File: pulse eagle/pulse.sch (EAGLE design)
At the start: 18 parts, among them J1 ISP Touch, U1 ATMEGA328P, Y1 16MHz

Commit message: Adding extra stem led and three extra petal leds. Needs routing.
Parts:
- added JP7, JP9: (no value), SparkFun-Connectors:M03POLAR_LOCK
- added JP8: M023.5MM_LOCK, SparkFun-Connectors:M023.5MM_LOCK
- added R3: 220, resistor:R-US_R0805
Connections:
- new net N$1: JP9.2, R3.2
- new net PETALWHITE: JP7.1, JP7.2, JP7.3, U1.PB1(OC1A)
- new net STEMLED2: R3.1, U1.PD7(AIN1)
- net 12V: now also JP8.2
- net GND: now also JP8.1, JP9.1
- net STEMLED: now also U1.PB0(ICP); no longer U1.PB1(OC1A)
- net VCC: now also JP9.3
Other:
- moved on the sheet: JP1, JP2, JP3, JP4, R1, SL2

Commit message: Revision 5 of the board, with 4 x Petals, 2 x Stem.
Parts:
- JP1: value (none) -> Power
- JP4, JP9: value (none) -> Stem
- JP6: value M023.5MM_LOCK -> Petal Center
- JP8: value M023.5MM_LOCK -> Petal Color
- SL2: value (none) -> Pulse Sensor
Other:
- note added: "Pulse & Bloom, 2014"
- moved on the sheet: C1, C10, C11, J1, JP1, JP2, JP3, JP4, JP7, JP8, R1, R2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

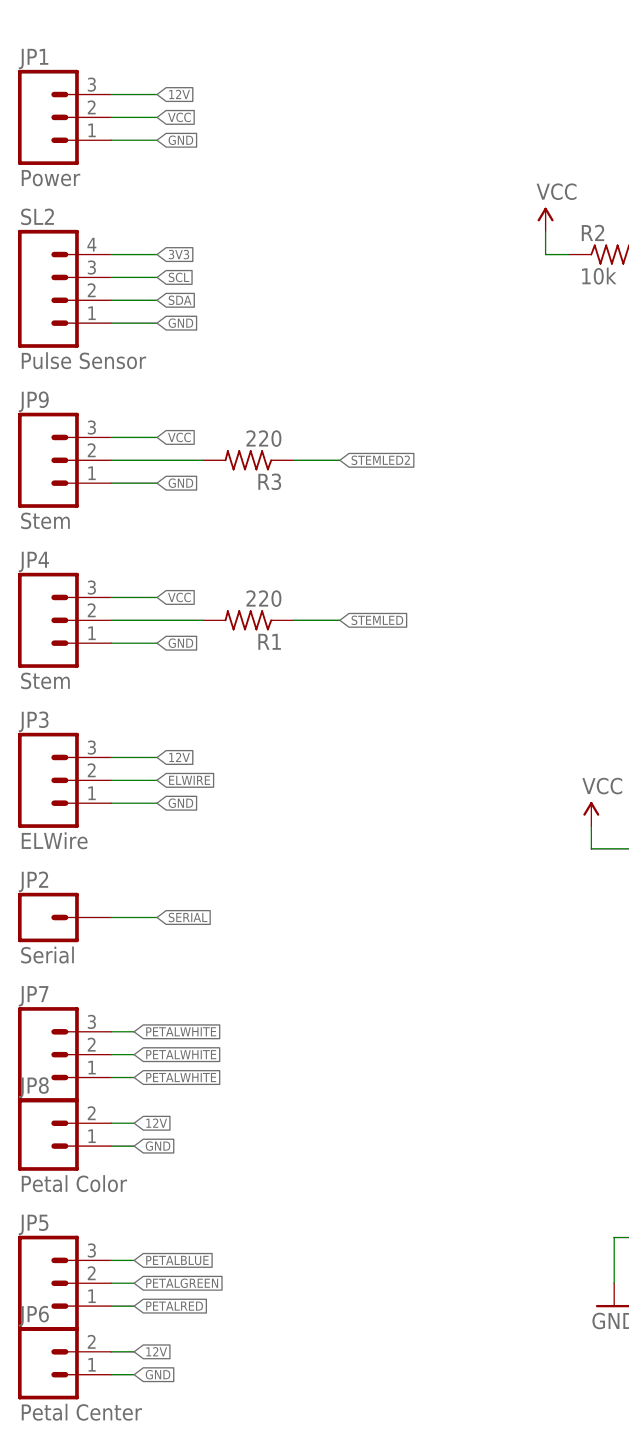
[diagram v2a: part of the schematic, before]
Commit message: Adding extra gnd pins for picobucks. probably going to need more picobucks.
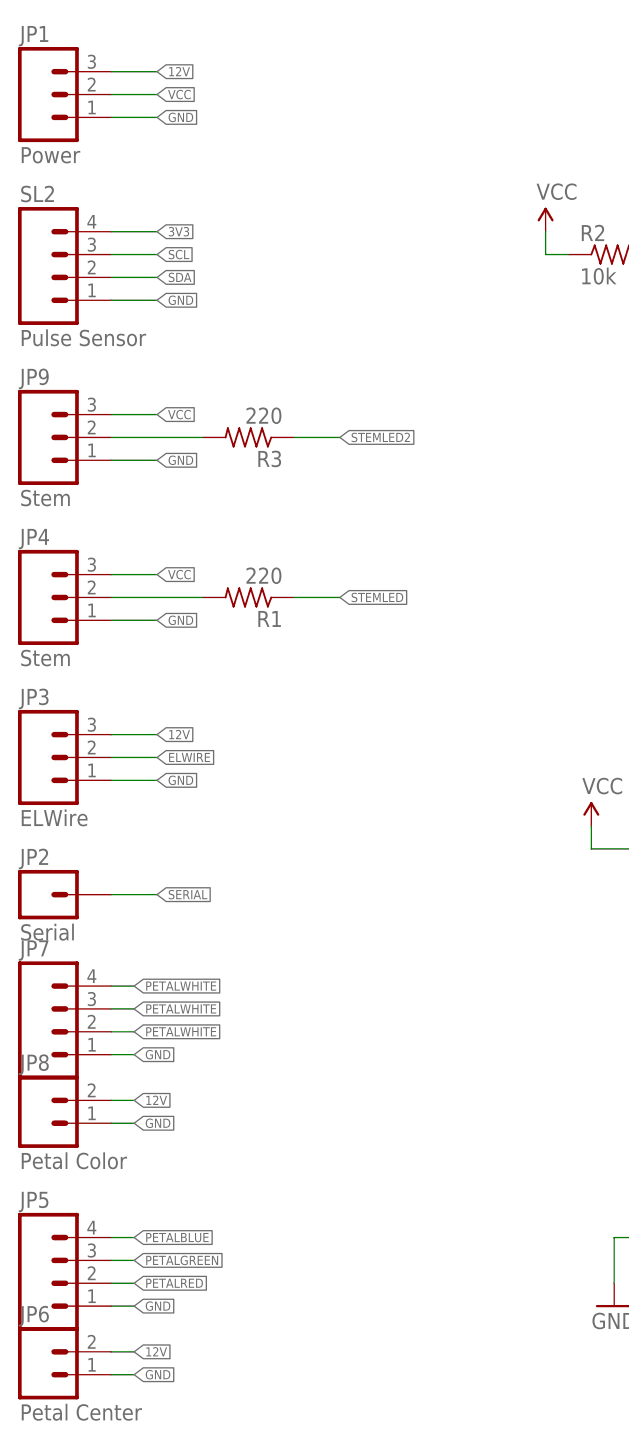
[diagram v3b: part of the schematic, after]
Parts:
- JP5: device SparkFun-Connectors:M03POLAR_LOCK -> SparkFun-Connectors:M04POLAR_LOCK
- JP7: device SparkFun-Connectors:M03POLAR_LOCK -> SparkFun-Connectors:M04POLAR
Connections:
- net GND: now also JP5.1, JP7.1
- net PETALBLUE: now also JP5.4; no longer JP5.3
- net PETALGREEN: now also JP5.3; no longer JP5.2
- net PETALRED: now also JP5.2; no longer JP5.1
- net PETALWHITE: now also JP7.4; no longer JP7.1
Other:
- moved on the sheet: JP1, JP2, JP3, JP4, JP8, JP9, R1, R3, SL2

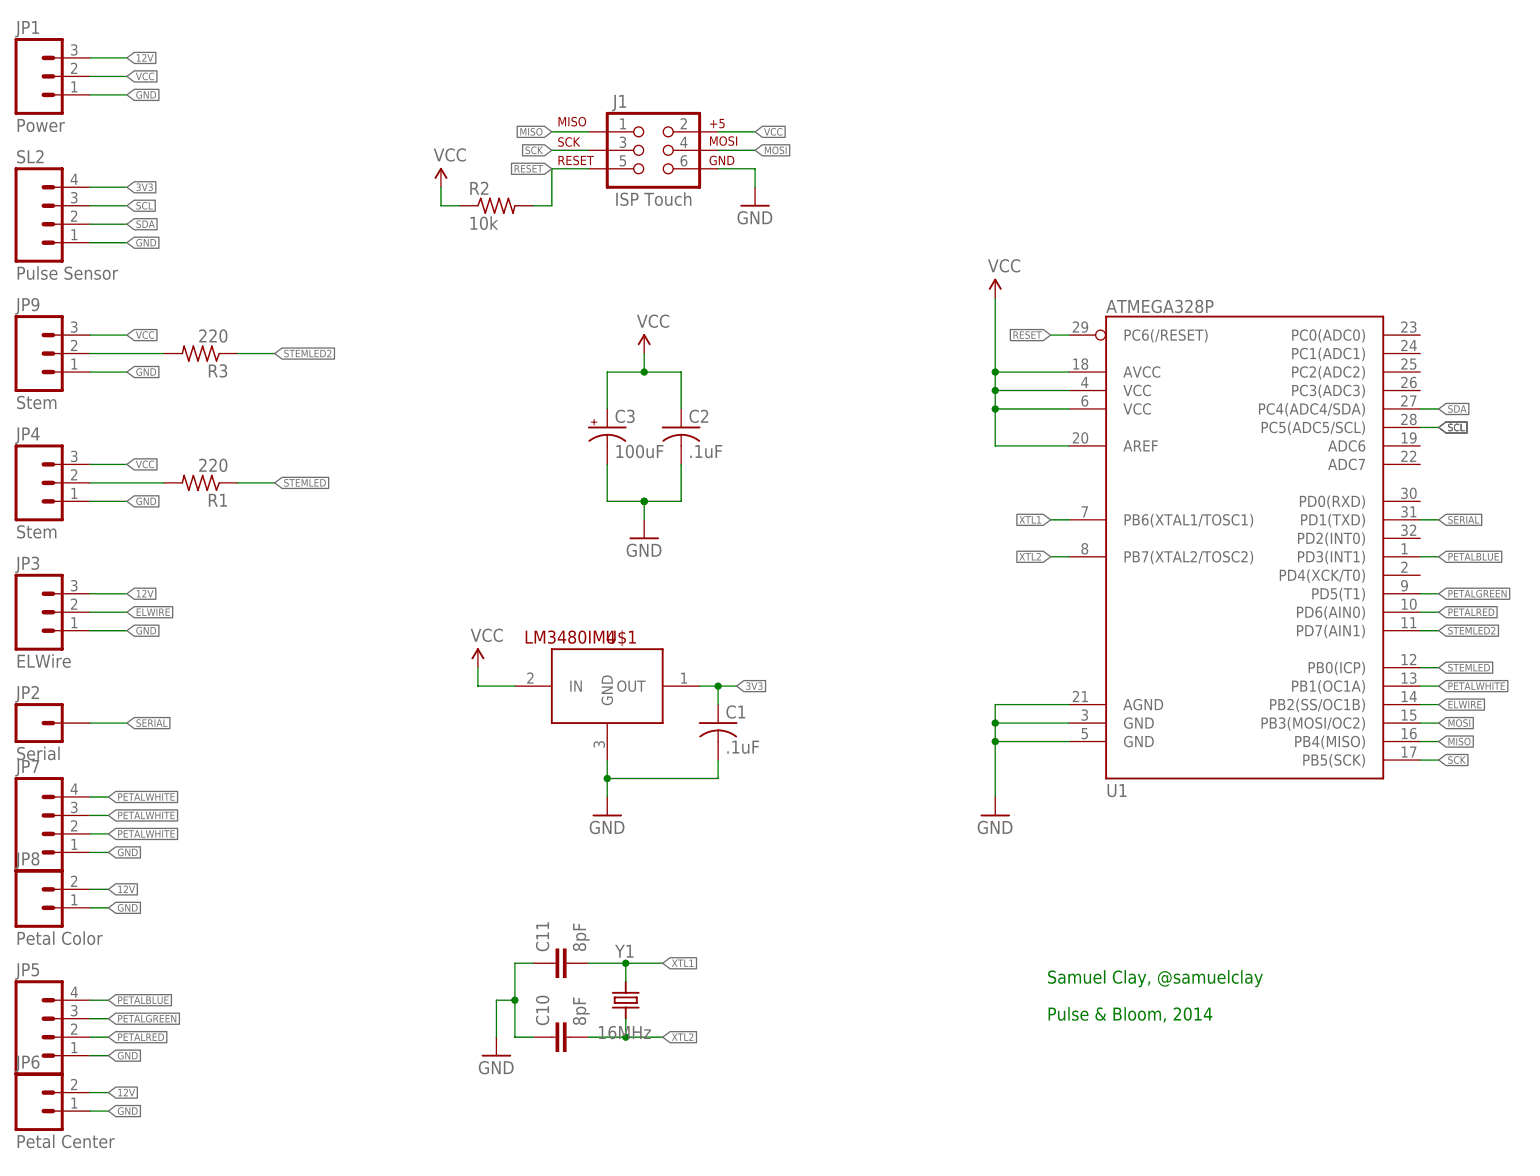
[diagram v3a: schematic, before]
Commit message: Adding second pulse sensor to board and code. Need to write code to handle second pulse sensor and second stem.
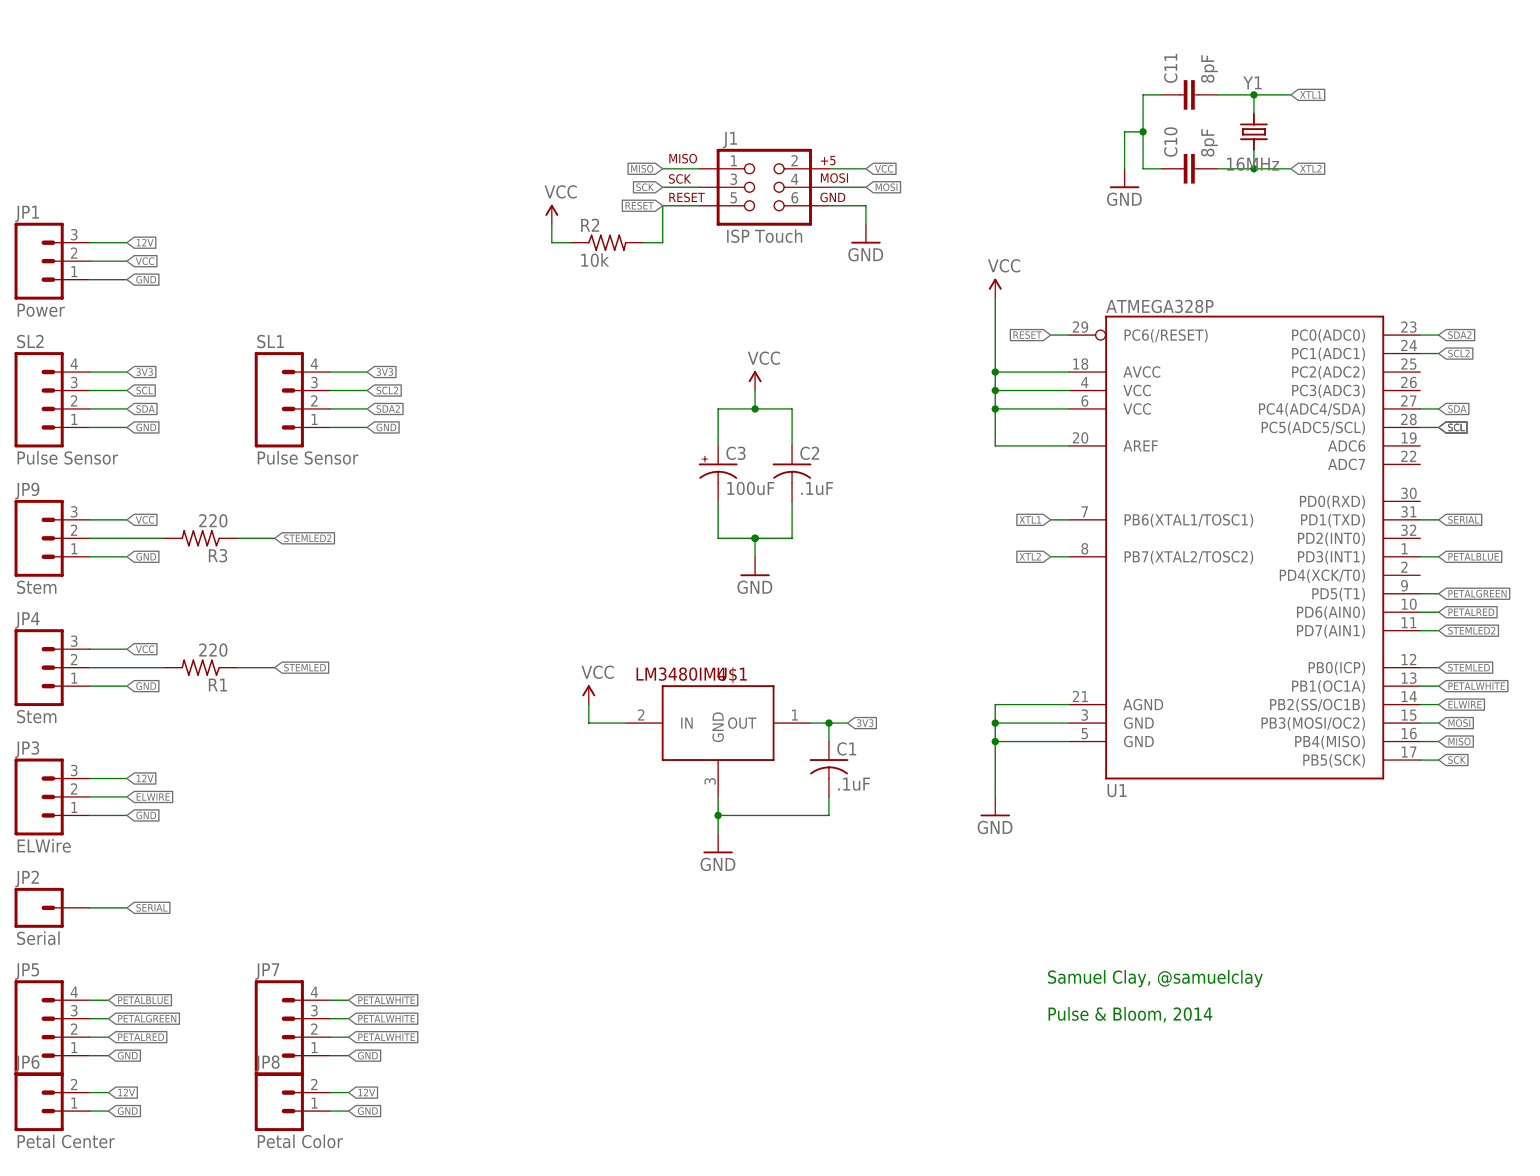
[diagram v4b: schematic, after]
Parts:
- added SL1: Pulse Sensor, SparkFun-Connectors:M04POLAR_LOCK
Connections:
- new net SCL2: SL1.3, U1.PC1(ADC1)
- new net SDA2: SL1.2, U1.PC0(ADC0)
- net 3V3: now also SL1.4
- net GND: now also SL1.1
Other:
- moved on the sheet: C1, C10, C11, C2, C3, J1, JP1, JP2, JP3, JP4, JP7, JP8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

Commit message: Adding a barrel jack and proper buck converter connectors.
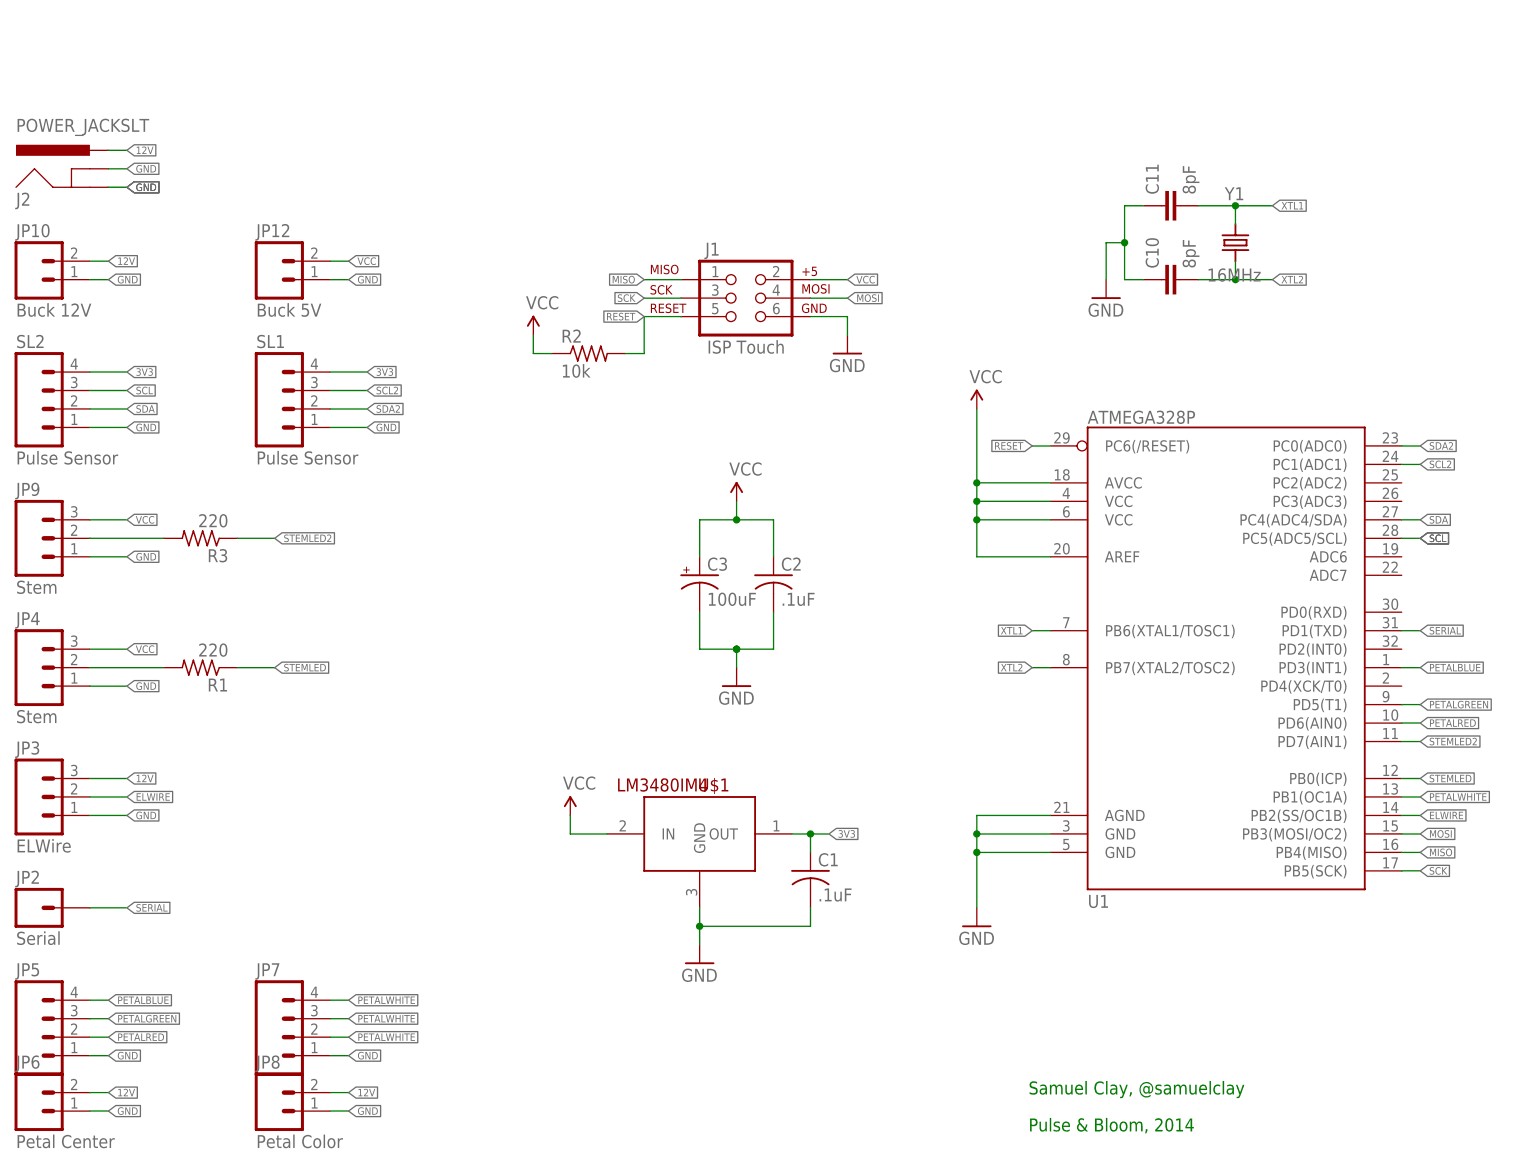
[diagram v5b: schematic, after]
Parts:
- removed JP1: Power, SparkFun-Connectors:M03SCREW_LOCK
- added J2: POWER_JACKSLT, SparkFun-Connectors:POWER_JACKSLT
- added JP10: Buck 12V, SparkFun-Connectors:M023.5MM_LOCK
- added JP12: Buck 5V, SparkFun-Connectors:M023.5MM_LOCK
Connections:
- net 12V: now also J2.PWR, JP10.2; no longer JP1.3
- net GND: now also J2.GND, J2.GNDBREAK, JP10.1, JP12.1; no longer JP1.1
- net VCC: now also JP12.2; no longer JP1.2
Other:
- moved on the sheet: C1, C10, C11, C2, C3, J1, R2, U$1, U1, Y1
